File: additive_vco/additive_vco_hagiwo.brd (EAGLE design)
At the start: 28.1 x 107.5 mm, 41 parts, among them IC1 MCP6232, J1 THONKICONNNEW, J2 THONKICONNNEW, J3 THONKICONNNEW, J4 THONKICONNNEW, M1 ARDUINO-NANO-3.0

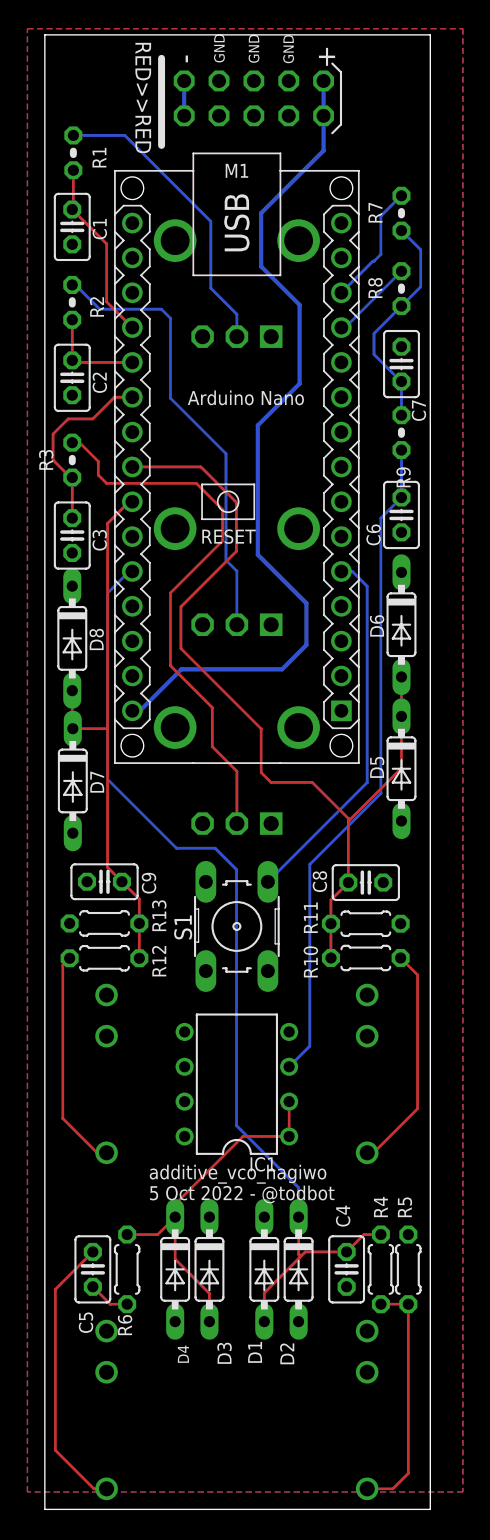
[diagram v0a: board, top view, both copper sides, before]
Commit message: skooch layout a bit to USB and power work out
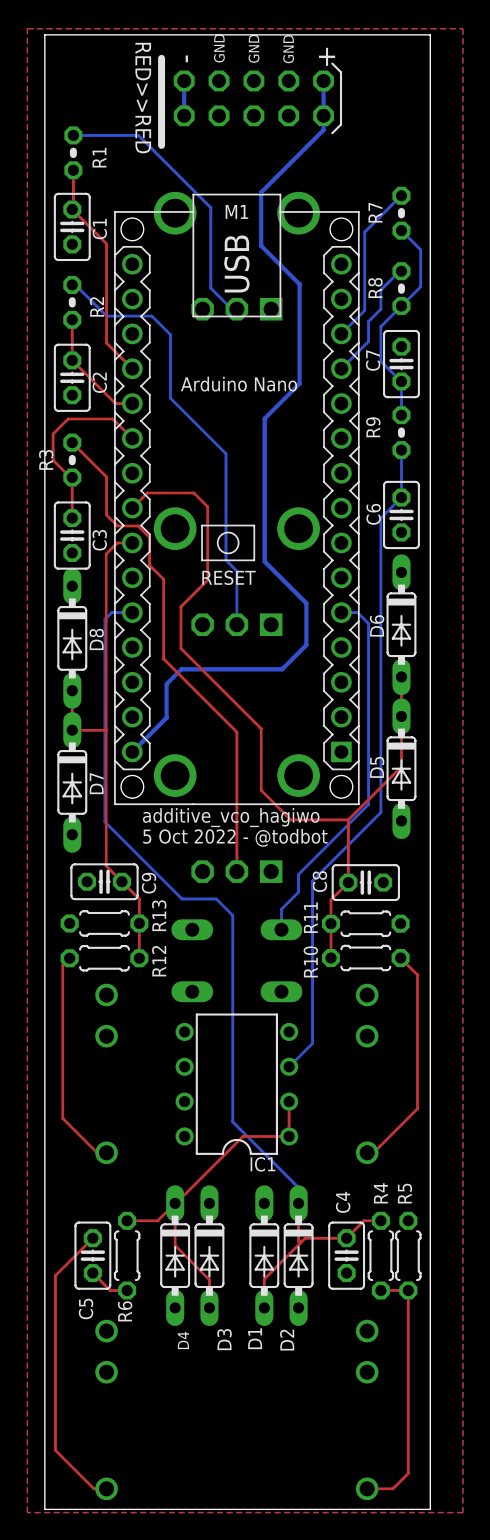
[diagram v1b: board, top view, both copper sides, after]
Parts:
- moved VR3 3.50 mm to (14.0, 53.5)
- moved M1 3.00 mm to (14.0, 73.0)
- moved S1 2.50 mm to (14.0, 40.0), flipped to the bottom, turned to 0 degrees
- moved VR1 2.00 mm to (14.0, 94.5)
- moved C4 1.00 mm to (22.0, 18.5)
- moved C5 1.00 mm to (3.50, 18.5)
- moved D1 1.00 mm to (16.0, 18.5)
- moved D2 1.00 mm to (18.5, 18.5)
- moved D3 1.00 mm to (12.0, 18.5)
- moved D4 1.00 mm to (9.50, 18.5)
- moved R4 1.00 mm to (24.5, 18.5)
- moved R5 1.00 mm to (26.5, 18.5)
- moved R6 1.00 mm to (6.00, 18.5)
- moved D7 0.12 mm to (2.00, 53.0)
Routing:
- net A7: track 70.8 -> 67.5 mm
- net A0: track 13.3 -> 16.3 mm
- net D10: track 8.95 -> 11.9 mm
- net D9: track 6.08 -> 9.00 mm
- net N$3: track 40.0 -> 37.1 mm
- net A4: track 63.0 -> 60.1 mm
- net A5: track 40.4 -> 38.1 mm
- net +12V: track 61.6 -> 63.8 mm
- net A1: track 7.40 -> 8.64 mm
- net N$1: track 21.8 -> 20.6 mm
- net N$7: track 17.8 -> 18.8 mm
- net N$5: track 20.5 -> 21.5 mm
- net N$6: track 26.5 -> 25.6 mm
- net N$2: track 32.5 -> 31.8 mm
